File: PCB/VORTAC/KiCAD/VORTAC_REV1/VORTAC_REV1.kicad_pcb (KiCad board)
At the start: 4 copper layers, 68.4 x 24.7 mm, 84 parts, among them IC1 TMC2209-LA, J1 DEBUG, J14 918-418K2023S40001, J15 STEPPER, J3 Conn_01x05, SW1 Boot, SW2 Reset, U1 TLV73333PDBV, U2 STM32F103C8T6, U3 EE-SX4350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

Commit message: Hallo
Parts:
- removed C44: 10nF, Capacitor_SMD:C_0402_1005Metric
- removed C45: 1uF, Capacitor_SMD:C_0402_1005Metric
- removed L3: 10uH 15mA, Inductor_SMD:L_0805_2012Metric
- removed R33: 10K, Resistor_SMD:R_0402_1005Metric
- added C19: 0.1uF 16V, Capacitor_SMD:C_0402_1005Metric, F.Cu at (139.6, 100.8)
- added C25: 0.1uF 16V, Capacitor_SMD:C_0402_1005Metric, F.Cu at (139.6, 102.8)
- added R13: 1K, Resistor_SMD:R_0402_1005Metric, F.Cu at (144.5, 100.8)
- added R14: 10K, Resistor_SMD:R_0402_1005Metric, F.Cu at (139.6, 98.9)
- J15: footprint Connector_JST:JST_PH_B4B-PH-K_1x04_P2.00mm_Vertical -> Vortac:JST_PH_S4B-PH-K_1x04_P2.00mm_Horizontal; moved to B.Cu
- R9: value 100R -> 10K; moved to F.Cu
- moved IC1 32.6 mm to (154.3, 85.8)
- moved R9 21.4 mm to (144.5, 98.9), turned to 0 degrees
- moved J15 10.9 mm to (152.9, 114.7), turned to 90 degrees
- moved U3 0.50 mm to (149.5, 119.4)
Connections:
- J1 pad 1: BOOT_1 -> BOOT_0
- R9 pad 1: Net-(U2-PA15) -> NRST
- R9 pad 2: unconnected-(R9-Pad2) -> +3V3
- U2 pad 12: TMC_UART -> Net-(U2-PA2)
- U2 pad 38: Net-(U2-PA15) -> unconnected-(U2-PA15-Pad38)

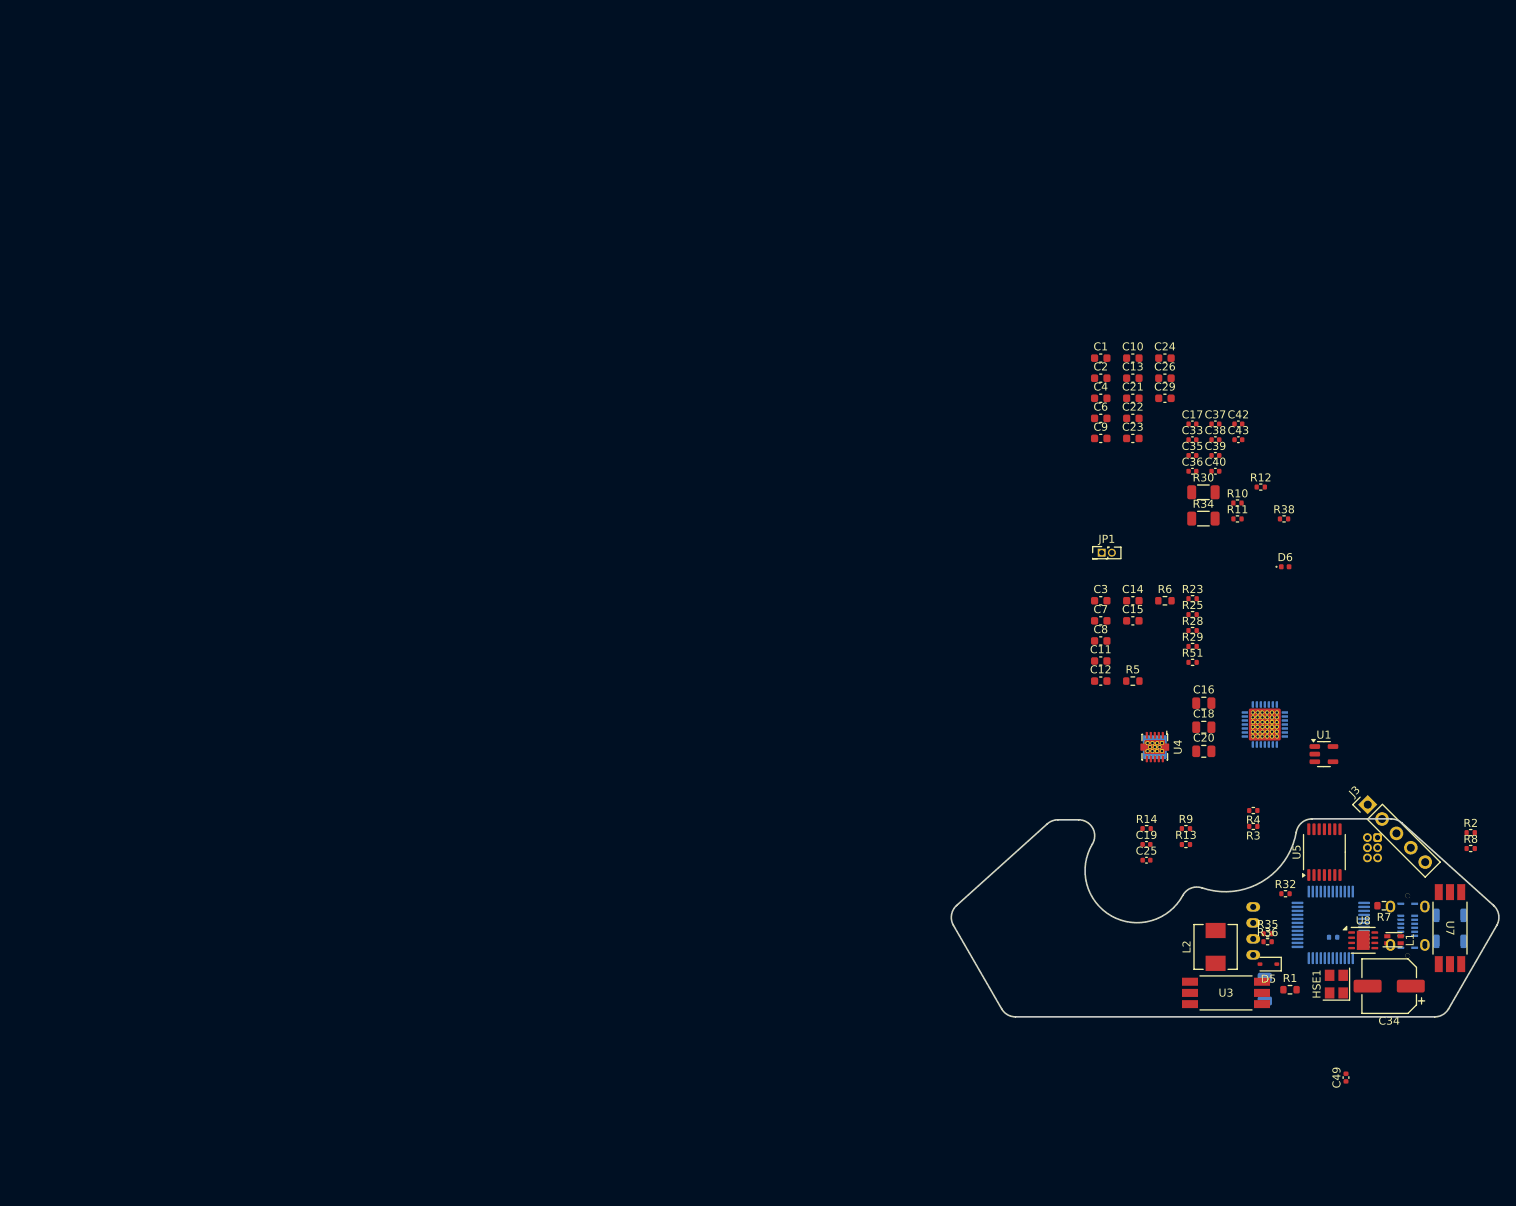
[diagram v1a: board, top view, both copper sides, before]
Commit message: Schematic updates
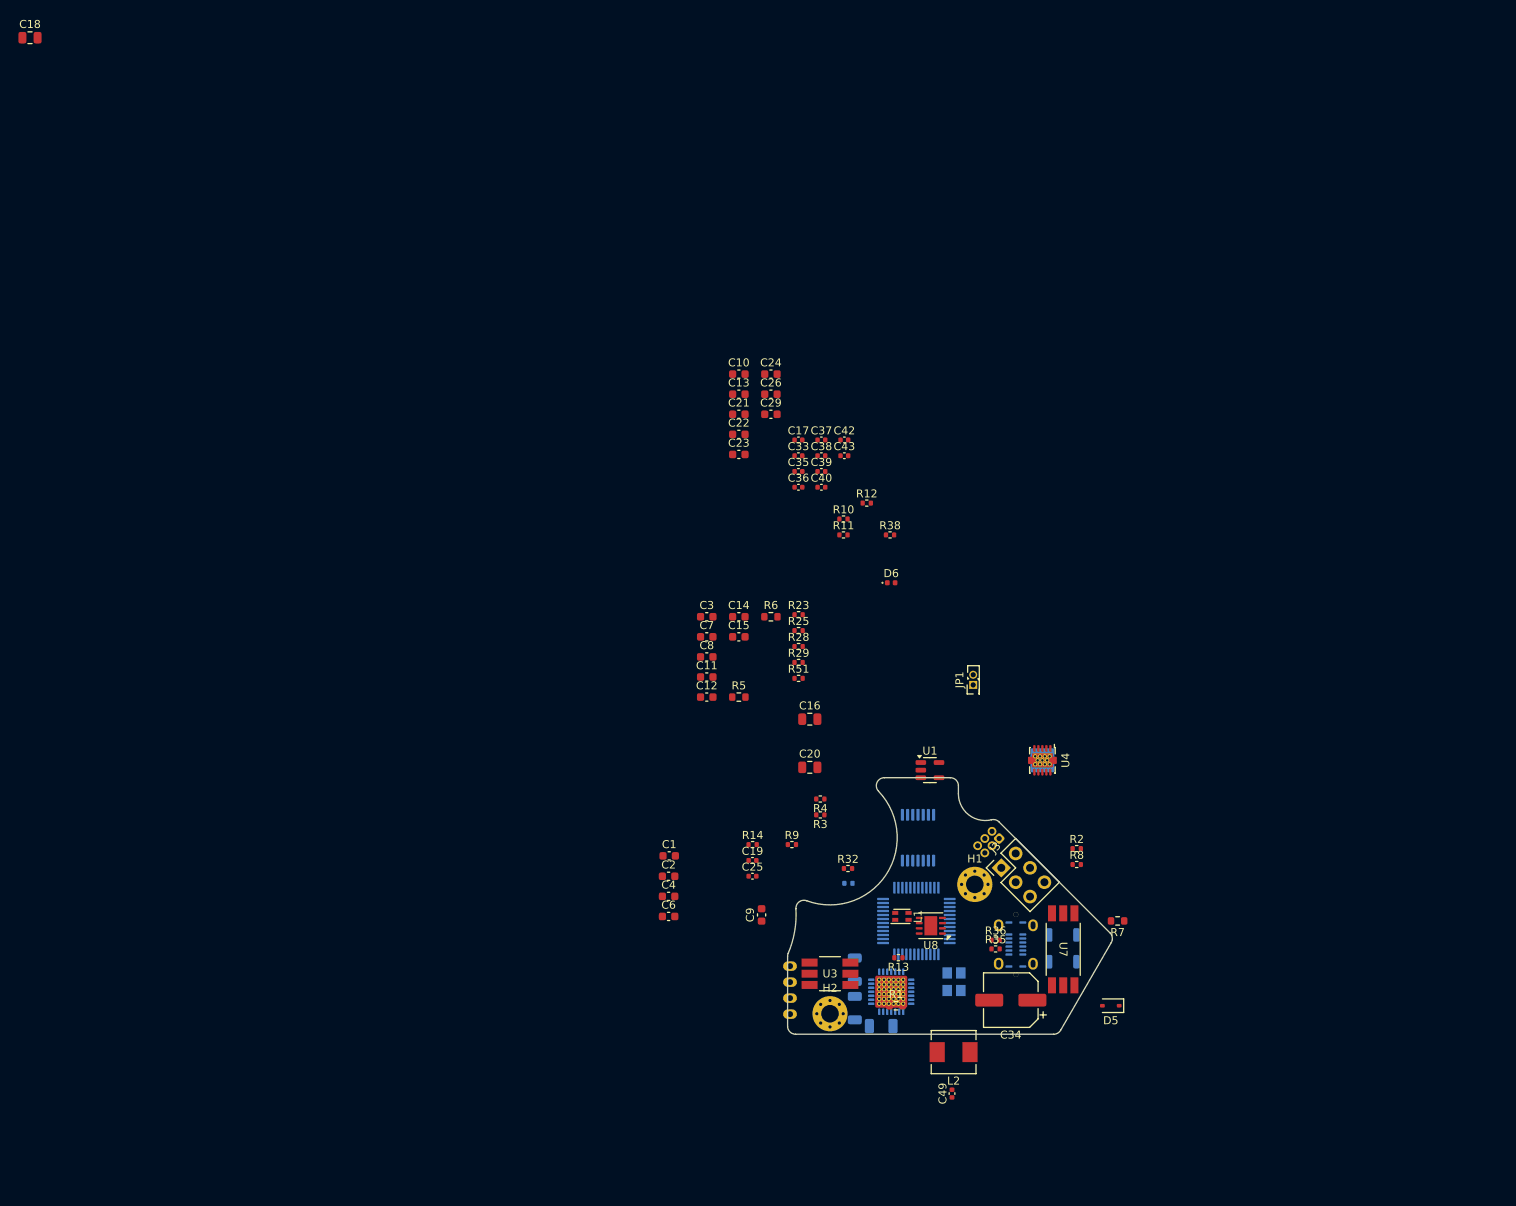
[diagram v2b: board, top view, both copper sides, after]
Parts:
- added H1: MountingHole_Pad, MountingHole:MountingHole_2.2mm_M2_Pad_Via, F.Cu at (118.1, 105.8)
- added H2: MountingHole_Pad, MountingHole:MountingHole_2.2mm_M2_Pad_Via, F.Cu at (100.0, 122.0)
- HSE1, R30, R34, U5: moved to B.Cu
- J3: footprint Connector_PinHeader_2.54mm:PinHeader_1x05_P2.54mm_Vertical -> Connector_PinHeader_2.54mm:PinHeader_2x03_P2.54mm_Vertical
- U3: value EE-SX4350 -> EE-SX4320; footprint Vortac:SENSOR_EE-SX3350_OMR -> Vortac:SENSOR_EE-SX4320_OMR
- U7: value EE-SX4350 -> EE-SX3350
- moved C18 170.2 mm to (0.00, 0.00)
- moved C6 82.4 mm to (79.8, 109.8)
- moved C2 82.4 mm to (79.8, 104.8)
- moved C4 82.4 mm to (79.8, 107.3)
- moved C1 82.3 mm to (79.9, 102.3)
- moved R34 75.1 mm to (103.1, 121.3), turned to 90 degrees
- moved R30 73.9 mm to (103.1, 116.5), turned to -90 degrees
- moved C9 73.1 mm to (91.5, 109.7), turned to 90 degrees
- moved L1 61.6 mm to (109.0, 109.8)
- moved R52 61.0 mm to (102.3, 105.7)
- moved J15 58.4 mm to (95.0, 122.0)
- moved IC1 57.4 mm to (107.7, 119.2), turned to -90 degrees
- moved R32 54.8 mm to (102.2, 103.8)
- moved R3 54.1 mm to (98.8, 97.2)
- moved R4 54.1 mm to (98.8, 95.2)
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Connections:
- R1 pad 1: Net-(U3-OUTPUT) -> unconnected-(R1-Pad1)
- R7 pad 1: Net-(U7-OUTPUT) -> unconnected-(R7-Pad1)
- U3 pad 4: +5V -> GND
- U3 pad 5: Net-(U3-OUTPUT) -> +5V
- U3 pad 6: GND -> unconnected-(U3-OUTPUT-Pad6)
- U7 pad 5: Net-(U7-OUTPUT) -> unconnected-(U7-OUTPUT-Pad5)
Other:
- board size 68.4 x 24.7 mm -> 40.6 x 32.1 mm

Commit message: Schematic Updates - Changed the 5V Rail to a more space efficient implementation
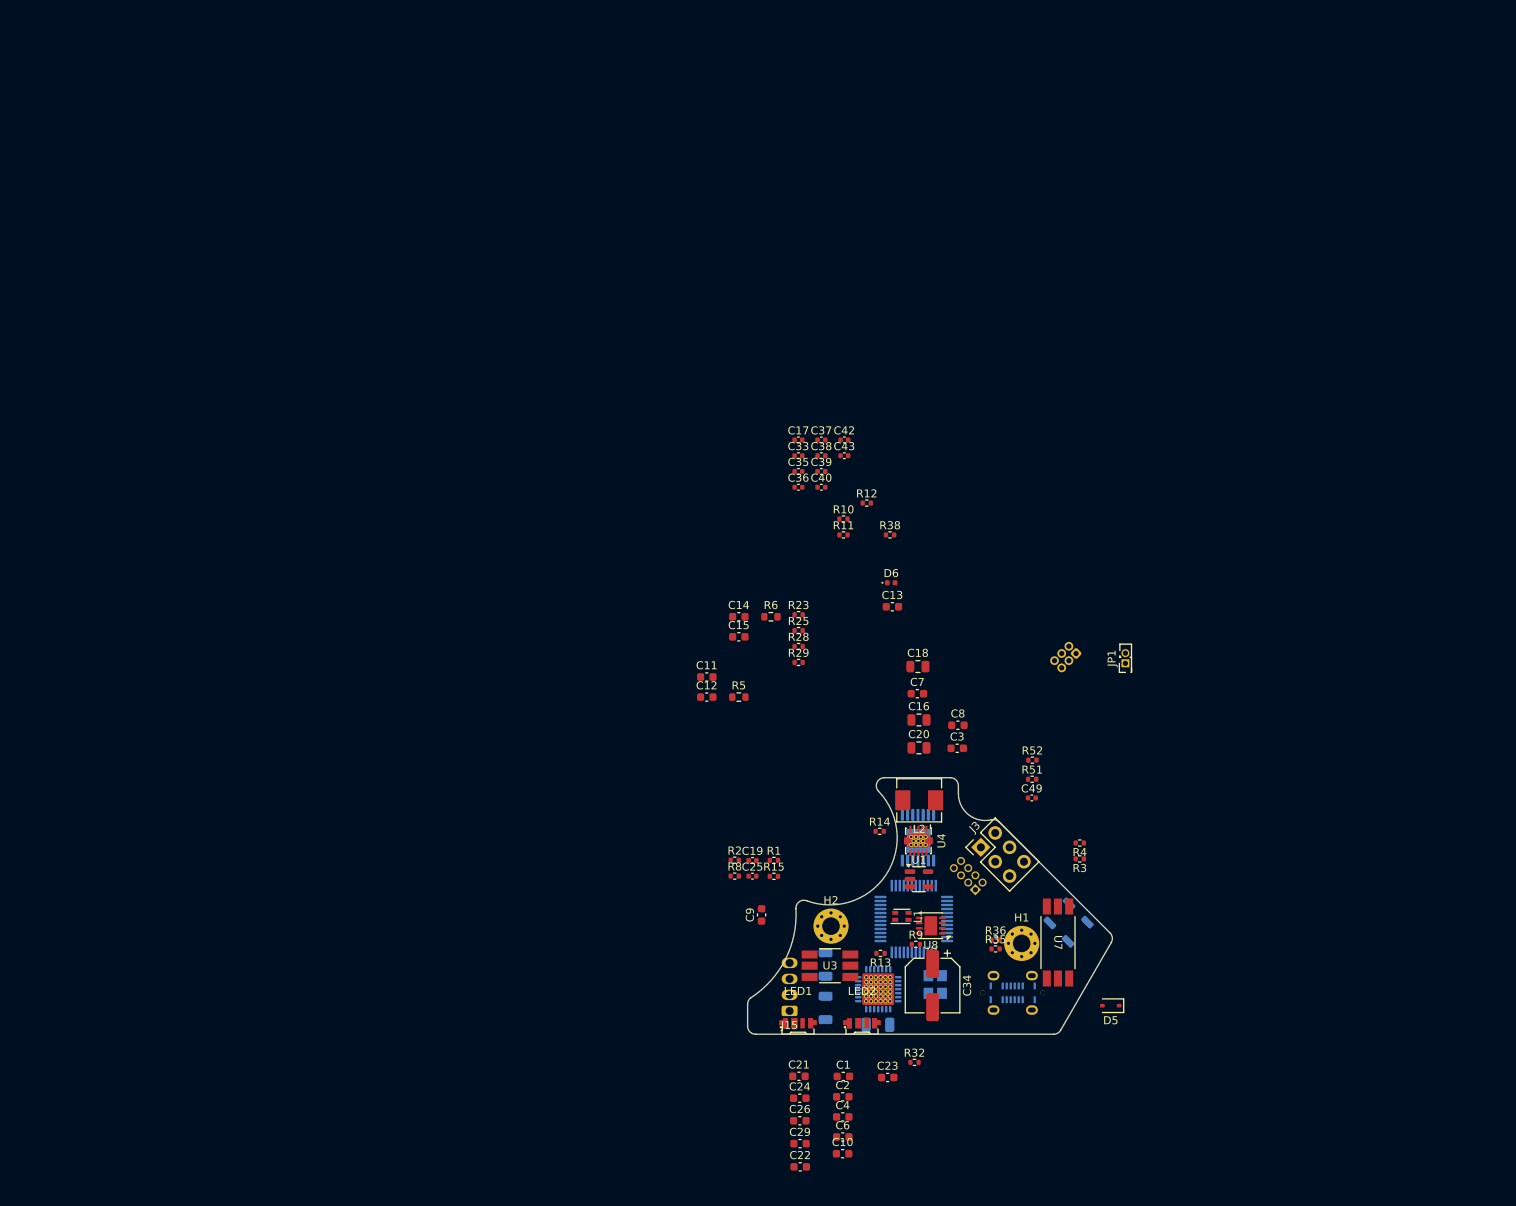
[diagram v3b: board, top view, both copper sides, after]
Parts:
- removed R7: 1K, Resistor_SMD:R_0603_1608Metric
- added J2: DEBUG, Connector_PinHeader_1.27mm:PinHeader_2x04_P1.27mm_Vertical, B.Cu at (118.2, 106.5)
- added LED1: SK6812SIDE-A-RVS, Vortac:LED-SMD_4P-L4.0-W1.6-L, F.Cu at (96.0, 123.2)
- added LED2: SK6812SIDE-A-RVS, Vortac:LED-SMD_4P-L4.0-W1.6-L, F.Cu at (104.0, 123.2)
- added R15: 1K, Resistor_SMD:R_0402_1005Metric, F.Cu at (93.0, 104.8)
- J15: footprint Vortac:JST_PH_S4B-PH-K_1x04_P2.00mm_Horizontal -> Vortac:Motor_Hand_Wire_pads; moved to F.Cu
- R1: footprint Resistor_SMD:R_0603_1608Metric -> Resistor_SMD:R_0402_1005Metric
- R52: moved to F.Cu
- moved C18 136.0 mm to (111.0, 78.6)
- moved C10 98.3 mm to (101.6, 139.5)
- moved C22 91.9 mm to (96.3, 141.1)
- moved C29 91.2 mm to (96.3, 138.2)
- moved C26 90.9 mm to (96.2, 135.4)
- moved C24 90.6 mm to (96.2, 132.6)
- moved C21 83.1 mm to (96.1, 129.8)
- moved C23 80.1 mm to (107.2, 130.0)
- moved R2 42.8 mm to (88.1, 102.8)
- moved R8 42.8 mm to (88.1, 104.8)
- moved C49 38.3 mm to (125.2, 95.0), turned to 0 degrees
- moved C3 35.4 mm to (115.9, 88.8)
- moved C1 35.1 mm to (101.7, 129.8)
- moved C4 35.1 mm to (101.6, 134.9)
- moved C2 35.1 mm to (101.6, 132.4)
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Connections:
- R1 pad 1: unconnected-(R1-Pad1) -> ENDSTOP_Z
- R1 pad 2: ENDSTOP_Z -> Net-(U3-OUTPUT)
- U3 pad 6: unconnected-(U3-OUTPUT-Pad6) -> Net-(U3-OUTPUT)
- U7 pad 5: unconnected-(U7-OUTPUT-Pad5) -> Net-(U7-OUTPUT)
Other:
- board size 40.6 x 32.1 mm -> 45.6 x 32.1 mm

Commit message: Schematic Updates Madrilla
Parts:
- added C27: 10uF 50V, Capacitor_SMD:C_1206_3216Metric, F.Cu at (159.7, 99.1)
- added C28: 0.1uF 50V, Capacitor_SMD:C_0603_1608Metric, F.Cu at (158.9, 101.7)
- added C30: 22uF, Capacitor_SMD:C_0805_2012Metric, F.Cu at (159.3, 93.6)
- added C31: 22uF, Capacitor_SMD:C_0805_2012Metric, F.Cu at (159.3, 96.6)
- added L3: 4.7uH, Vortac:L_Sunlord_MWSA0518_5.4x5.2mm, F.Cu at (153.8, 99.5)
- added R7: 100R, Resistor_SMD:R_0402_1005Metric, F.Cu at (96.9, 121.1)
- added U6: AP63205WU, Package_TO_SOT_SMD:TSOT-23-6, F.Cu at (153.3, 93.9)
- C5: moved to F.Cu
- moved C12 96.4 mm to (180.1, 95.3)
- moved C11 94.4 mm to (176.2, 102.7)
- moved C14 93.3 mm to (176.2, 104.4)
- moved C17 91.8 mm to (147.7, 126.2)
- moved C35 90.5 mm to (147.5, 128.6)
- moved R23 88.2 mm to (180.6, 97.5)
- moved R25 88.0 mm to (180.6, 98.7)
- moved R28 87.8 mm to (180.5, 100.0)
- moved R29 87.5 mm to (180.5, 101.2)
- moved R10 84.3 mm to (147.5, 130.9)
- moved C5 75.3 mm to (176.9, 98.2), turned to 180 degrees
- moved C20 69.4 mm to (180.3, 93.1)
- moved C7 67.9 mm to (176.2, 100.9)
- moved C18 66.8 mm to (176.2, 93.2)
- moved C16 66.0 mm to (176.3, 95.6)
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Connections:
- LED1 pad 1: unconnected-(LED1-DIN-Pad1) -> LED_DIN
- LED1 pad 2: unconnected-(LED1-VDD-Pad2) -> +5V
- LED1 pad 3: unconnected-(LED1-DOUT-Pad3) -> Net-(LED1-DOUT)
- LED1 pad 4: unconnected-(LED1-GND-Pad4) -> GND
- LED2 pad 1: unconnected-(LED2-DIN-Pad1) -> Net-(LED1-DOUT)
- LED2 pad 2: unconnected-(LED2-VDD-Pad2) -> +5V
- LED2 pad 4: unconnected-(LED2-GND-Pad4) -> GND
- U2 pad 14: unconnected-(U2-PA4-Pad14) -> Net-(U2-PA4)
- U2 pad 16: unconnected-(U2-PA6-Pad16) -> ENDSTOP_Z
- U2 pad 17: unconnected-(U2-PA7-Pad17) -> ENDSTOP_X

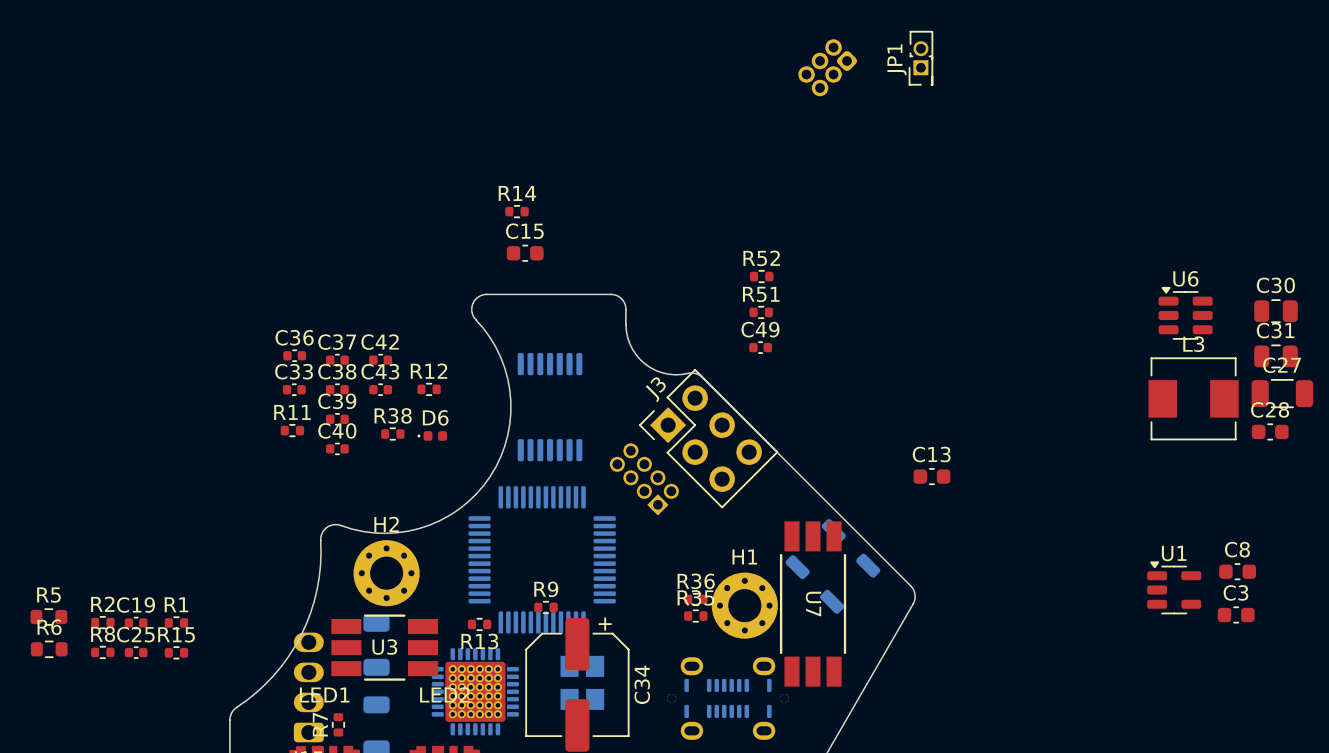
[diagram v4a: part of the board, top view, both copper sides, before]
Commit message: update to Kicad 9.0.X
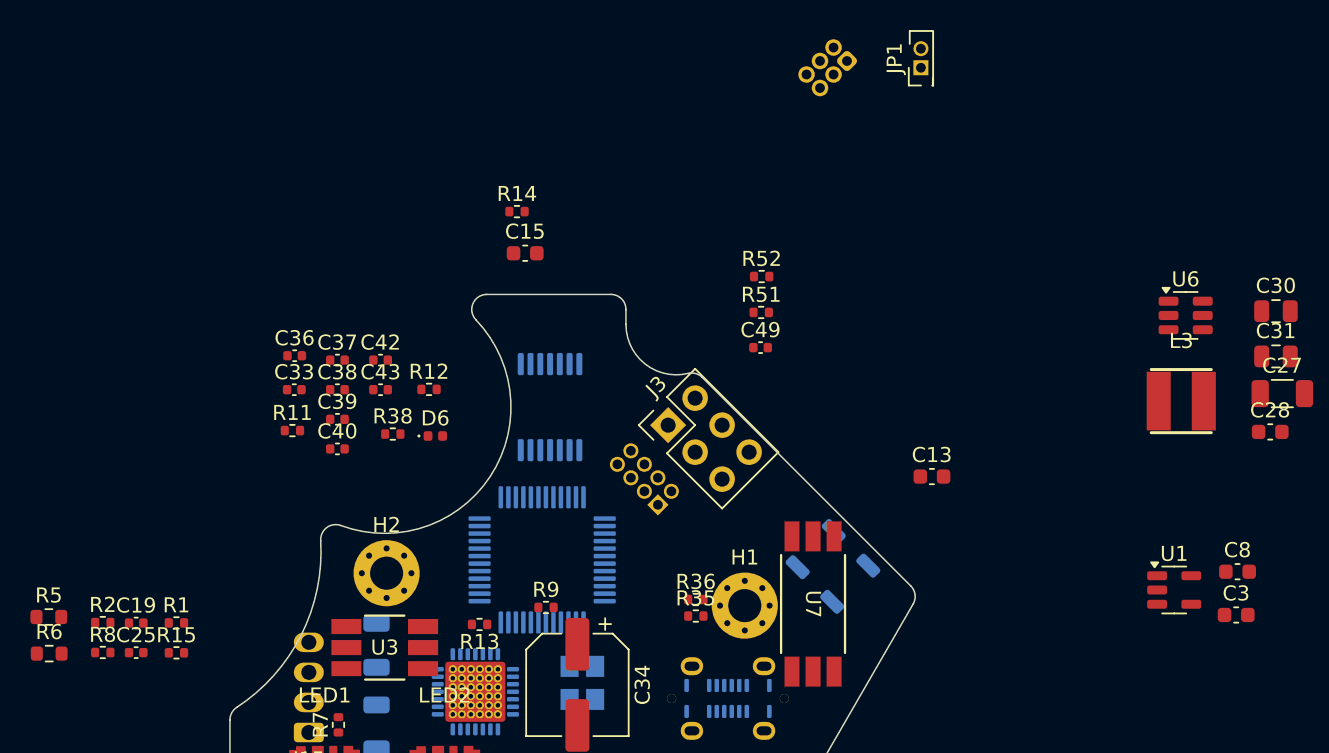
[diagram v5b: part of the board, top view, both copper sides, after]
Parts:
- L3: footprint Vortac:L_Sunlord_MWSA0518_5.4x5.2mm -> Vortac:IND-SMD_L4.0-W4.0_FNR40XXS
- moved L3 0.83 mm to (153.0, 99.6)
- moved R6 0.29 mm to (77.7, 116.4)

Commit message: pushy
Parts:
- removed C11, C7: 0.1uF 50V, Capacitor_SMD:C_0603_1608Metric
- removed C12: 3.3nF, Capacitor_SMD:C_0603_1608Metric
- removed C14: 56pF, Capacitor_SMD:C_0603_1608Metric
- removed C16, C18, C20: 47uF, Capacitor_SMD:C_0805_2012Metric
- removed C49: 0.1uF 16V, Capacitor_SMD:C_0402_1005Metric
- removed C5: 10uF 50V, Capacitor_SMD:C_1206_3216Metric
- removed L2: 10uH, Vortac:L_Sunlord_MWSA0518_5.4x5.2mm
- removed R23: 10k, Resistor_SMD:R_0402_1005Metric
- removed R25: 95k, Resistor_SMD:R_0402_1005Metric
- removed R28: 100k, Resistor_SMD:R_0402_1005Metric
- removed R29: 19.1k, Resistor_SMD:R_0402_1005Metric
- removed R51: 1K, Resistor_SMD:R_0402_1005Metric
- removed R52: 10K, Resistor_SMD:R_0402_1005Metric
- removed U4: TPS54335ADRCR, Vortac:VSON-10-1EP_3x3mm_P0.5mm_EP1.65x2.4mm_ThermalVias
